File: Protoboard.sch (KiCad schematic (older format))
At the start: 7 parts

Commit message: Updated footprints for most things.
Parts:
- added D1, D2: D, Diodes_SMD:SOD-323_HandSoldering, symbol D
- added R3: 10k, Resistors_SMD:R_1206_HandSoldering, symbol R
- P1: renamed from P?; footprint (none) -> Connectors_Molex:Molex_PicoBlade_53261-0871_08x1.25mm_Angled
- P2, P4: renamed from P?; footprint (none) -> Pin_Headers:Pin_Header_Straight_1x04
- P3: renamed from P?; footprint (none) -> Connectors_JST:JST_XH_S05B-XH-A_05x2.50mm_Angled
- R1, R2: renamed from R?; footprint (none) -> Resistors_SMD:R_1206_HandSoldering
- gave numbers to parts that had none: 1
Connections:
- net +3.3V: now also D1.1 (K)
- net +5V: now also R3.1
- new net DIN: D1.2 (A), D2.2 (A), R3.2
- new net LED: D2.1 (K)
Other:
- note added: "Level Converter for WS2812\n"
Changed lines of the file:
@@
 LIBS:contrib
 LIBS:valves
+LIBS:Protoboard-cache
 EELAYER 25 0
 EELAYER END
@@
 $EndDescr
 $Comp
-L CONN_01X04 P?
+L CONN_01X04 P2
 U 1 1 58C45125
 P 1000 1050
-F 0 "P?" H 1000 1300 50  0000 C CNN
+F 0 "P2" H 1000 1300 50  0000 C CNN
 F 1 "CONN_01X04" V 1100 1050 50  0000 C CNN
-F 2 "" H 1000 1050 50  0000 C CNN
+F 2 "Pin_Headers:Pin_Header_Straight_1x04" H 1000 1050 50  0001 C CNN
 F 3 "" H 1000 1050 50  0000 C CNN
 	1    1000 1050
@@
 $EndComp
 $Comp
-L CONN_01X04 P?
+L CONN_01X04 P4
 U 1 1 58C4517D
 P 1600 1600
-F 0 "P?" H 1600 1850 50  0000 C CNN
+F 0 "P4" H 1600 1850 50  0000 C CNN
 F 1 "CONN_01X04" V 1700 1600 50  0000 C CNN
-F 2 "" H 1600 1600 50  0000 C CNN
+F 2 "Pin_Headers:Pin_Header_Straight_1x04" H 1600 1600 50  0001 C CNN
 F 3 "" H 1600 1600 50  0000 C CNN
 	1    1600 1600
@@
 I2C Sensor Connector\n
 $Comp
-L CONN_01X05 P?
+L CONN_01X05 P3
 U 1 1 58C45292
 P 1000 2500
-F 0 "P?" H 1000 2800 50  0000 C CNN
+F 0 "P3" H 1000 2800 50  0000 C CNN
 F 1 "CONN_01X05" V 1100 2500 50  0000 C CNN
-F 2 "" H 1000 2500 50  0000 C CNN
+F 2 "Connectors_JST:JST_XH_S05B-XH-A_05x2.50mm_Angled" H 1000 2500 50  0001 C CNN
 F 3 "" H 1000 2500 50  0000 C CNN
 	1    1000 2500
@@
 SDS011 Connector\n
 $Comp
-L CONN_02X05 P?
+L CONN_02X05 P5
 U 1 1 58C453D9
 P 3300 4400
-F 0 "P?" H 3300 4700 50  0000 C CNN
+F 0 "P5" H 3300 4700 50  0000 C CNN
 F 1 "CONN_02X05" H 3300 4100 50  0000 C CNN
-F 2 "" H 3300 3200 50  0000 C CNN
+F 2 "" H 3300 3200 50  0001 C CNN
 F 3 "" H 3300 3200 50  0000 C CNN
 	1    3300 4400
@@
 PMS7003 Connector\n
 $Comp
-L CONN_01X08 P?
+L CONN_01X08 P1
 U 1 1 58C459C6
 P 950 6250
-F 0 "P?" H 950 6700 50  0000 C CNN
+F 0 "P1" H 950 6700 50  0000 C CNN
 F 1 "CONN_01X08" V 1050 6250 50  0000 C CNN
-F 2 "" H 950 6250 50  0000 C CNN
+F 2 "Connectors_Molex:Molex_PicoBlade_53261-0871_08x1.25mm_Angled" H 950 6250 50  0001 C CNN
 F 3 "" H 950 6250 50  0000 C CNN
 	1    950  6250
@@
 RESET
 $Comp
-L R R?
+L R R2
 U 1 1 58C4605C
 P 6150 1700
-F 0 "R?" V 6230 1700 50  0000 C CNN
+F 0 "R2" V 6230 1700 50  0000 C CNN
 F 1 "10k" V 6150 1700 50  0000 C CNN
-F 2 "" V 6080 1700 50  0000 C CNN
+F 2 "Resistors_SMD:R_1206_HandSoldering" V 6080 1700 50  0001 C CNN
 F 3 "" H 6150 1700 50  0000 C CNN
 	1    6150 1700
@@
 $EndComp
 $Comp
-L R R?
+L R R1
 U 1 1 58C4608F
 P 6150 1200
-F 0 "R?" V 6230 1200 50  0000 C CNN
+F 0 "R1" V 6230 1200 50  0000 C CNN
 F 1 "10k" V 6150 1200 50  0000 C CNN
-F 2 "" V 6080 1200 50  0000 C CNN
+F 2 "Resistors_SMD:R_1206_HandSoldering" V 6080 1200 50  0001 C CNN
 F 3 "" H 6150 1200 50  0000 C CNN
 	1    6150 1200
@@
 Text Notes 5400 950  0    60   ~ 0
 Pullups for PMS Sensors\n
+$Comp
+L D D1
+U 1 1 58C46C46
+P 6150 2500
+F 0 "D1" H 6150 2600 50  0000 C CNN
+F 1 "D" H 6150 2400 50  0000 C CNN
+F 2 "Diodes_SMD:SOD-323_HandSoldering" H 6150 2500 50  0001 C CNN
+F 3 "" H 6150 2500 50  0000 C CNN
+	1    6150 2500
+	1    0    0    -1
+$EndComp
+$Comp
+L D D2
+U 1 1 58C46CBC
+P 6150 3100
+F 0 "D2" H 6150 3200 50  0000 C CNN
+F 1 "D" H 6150 3000 50  0000 C CNN
+F 2 "Diodes_SMD:SOD-323_HandSoldering" H 6150 3100 50  0001 C CNN
+F 3 "" H 6150 3100 50  0000 C CNN
+	1    6150 3100
+	1    0    0    -1
+$EndComp
+Text GLabel 7200 3100 2    60   Input ~ 0
+DIN
+Text GLabel 7200 2500 2    60   Input ~ 0
++5V
+$Comp
+L R R3
+U 1 1 58C46D88
+P 6750 2500
+F 0 "R3" V 6830 2500 50  0000 C CNN
+F 1 "10k" V 6750 2500 50  0000 C CNN
+F 2 "Resistors_SMD:R_1206_HandSoldering" V 6680 2500 50  0001 C CNN
+F 3 "" H 6750 2500 50  0000 C CNN
+	1    6750 2500
+	0    1    1    0
+$EndComp
+Wire Wire Line
+	6900 2500 7200 2500
+Wire Wire Line
+	6600 2500 6300 2500
+Wire Wire Line
+	6300 3100 7200 3100
+Wire Wire Line
+	6450 2500 6450 3100
+Connection ~ 6450 3100
+Connection ~ 6450 2500
+Text GLabel 5400 2500 0    60   Input ~ 0
++3.3V
+Wire Wire Line
+	5400 2500 6000 2500
+Text GLabel 5400 3100 0    60   Input ~ 0
+LED
+Wire Wire Line
+	5400 3100 6000 3100
+Text Notes 5250 2300 0    60   ~ 0
+Level Converter for WS2812\n
 $EndSCHEMATC

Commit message: Added a drawing for RS part no http://uk.rs-online.com/web/p/pcb-sockets/7944590/?sra=pstk
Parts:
- P5: footprint (none) -> Amphenol:Amphenol
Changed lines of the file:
@@
 F 0 "P5" H 3300 4700 50  0000 C CNN
 F 1 "CONN_02X05" H 3300 4100 50  0000 C CNN
-F 2 "" H 3300 3200 50  0001 C CNN
+F 2 "Amphenol:Amphenol" H 3300 3200 50  0001 C CNN
 F 3 "" H 3300 3200 50  0000 C CNN
 	1    3300 4400

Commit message: WIP
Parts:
- added P6: CONN_01X10, Pin_Headers:Pin_Header_Straight_1x10, symbol CONN_01X10
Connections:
- net +3.3V: now also P6.3 (P3)
- net +5V: now also P6.4 (P4)
- net DIN: now also P6.10 (P10)
- net GND: now also P6.5 (P5)
- net RESET: now also P6.9 (P9)
- net RXD: now also P6.7 (P7)
- net SCL: now also P6.1 (P1)
- net SDA: now also P6.2 (P2)
- net SET: now also P6.8 (P8)
- net TXD: now also P6.6 (P6)
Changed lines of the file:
@@
 Text Notes 5250 2300 0    60   ~ 0
 Level Converter for WS2812\n
+Text GLabel 8100 3450 0    60   Input ~ 0
+SCL
+Text GLabel 8100 3600 0    60   Input ~ 0
+SDA
+Text GLabel 8100 3750 0    60   Input ~ 0
++3.3V
+Text GLabel 8100 3900 0    60   Input ~ 0
++5V
+Text GLabel 8100 4050 0    60   Input ~ 0
+GND
+Text GLabel 8100 4200 0    60   Input ~ 0
+TXD
+Text GLabel 8100 4350 0    60   Input ~ 0
+RXD
+Text GLabel 8100 4500 0    60   Input ~ 0
+SET
+Text GLabel 8100 4650 0    60   Input ~ 0
+RESET
+Text GLabel 8100 4800 0    60   Input ~ 0
+DIN
+$Comp
+L CONN_01X10 P6
+U 1 1 58C59B8A
+P 9350 4150
+F 0 "P6" H 9350 4700 50  0000 C CNN
+F 1 "CONN_01X10" V 9450 4150 50  0000 C CNN
+F 2 "Pin_Headers:Pin_Header_Straight_1x10" H 9350 4150 50  0001 C CNN
+F 3 "" H 9350 4150 50  0000 C CNN
+	1    9350 4150
+	1    0    0    -1
+$EndComp
+Wire Wire Line
+	9150 3700 9050 3700
+Wire Wire Line
+	9050 3700 9050 3450
+Wire Wire Line
+	9050 3450 8100 3450
+Wire Wire Line
+	9150 3800 8950 3800
+Wire Wire Line
+	8950 3800 8950 3600
+Wire Wire Line
+	8950 3600 8100 3600
+Wire Wire Line
+	9150 3900 8850 3900
+Wire Wire Line
+	8850 3900 8850 3750
+Wire Wire Line
+	8850 3750 8100 3750
+Wire Wire Line
+	9150 4000 8750 4000
+Wire Wire Line
+	8750 4000 8750 3900
+Wire Wire Line
+	8750 3900 8100 3900
+Wire Wire Line
+	9150 4100 8650 4100
+Wire Wire Line
+	8650 4100 8650 4050
+Wire Wire Line
+	8650 4050 8100 4050
+Wire Wire Line
+	9150 4200 8100 4200
+Wire Wire Line
+	9150 4300 8650 4300
+Wire Wire Line
+	8650 4300 8650 4350
+Wire Wire Line
+	8650 4350 8100 4350
+Wire Wire Line
+	9150 4400 8750 4400
+Wire Wire Line
+	8750 4400 8750 4500
+Wire Wire Line
+	8750 4500 8100 4500
+Wire Wire Line
+	9150 4500 8850 4500
+Wire Wire Line
+	8850 4500 8850 4650
+Wire Wire Line
+	8850 4650 8100 4650
+Wire Wire Line
+	9150 4600 8950 4600
+Wire Wire Line
+	8950 4600 8950 4800
+Wire Wire Line
+	8950 4800 8100 4800
 $EndSCHEMATC

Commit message: Routing done.
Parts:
- removed P4: CONN_01X04, Pin_Headers:Pin_Header_Straight_1x04, symbol CONN_01X04
- removed P6: CONN_01X10, Pin_Headers:Pin_Header_Straight_1x10, symbol CONN_01X10
- added P4: CONN_01X11, Pin_Headers:Pin_Header_Straight_1x11, symbol CONN_01X11
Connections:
- net +3.3V: now also P4.3 (P3)
- net +5V: now also P4.5 (P5)
- net DIN: now also P4.10 (P10)
- net GND: now also P4.4 (P4)
- net LED: now also P4.11 (P11)
- net RESET: now also P4.9 (P9)
- net RXD: now also P4.7 (P7)
- net SCL: now also P4.1 (P1)
- net SDA: now also P4.2 (P2)
- net SET: now also P4.6 (P6)
- net TXD: now also P4.8 (P8)
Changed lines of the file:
@@
 	-1   0    0    1
-$EndComp
-$Comp
-L CONN_01X04 P4
-U 1 1 58C4517D
-P 1600 1600
-F 0 "P4" H 1600 1850 50  0000 C CNN
-F 1 "CONN_01X04" V 1700 1600 50  0000 C CNN
-F 2 "Pin_Headers:Pin_Header_Straight_1x04" H 1600 1600 50  0001 C CNN
-F 3 "" H 1600 1600 50  0000 C CNN
-	1    1600 1600
-	0    1    1    0
 $EndComp
 Text GLabel 2400 1200 2    60   Input ~ 0
@@
 	1200 1200 2400 1200
 Wire Wire Line
-	1750 1400 1750 1200
-Connection ~ 1750 1200
-Wire Wire Line
 	1200 1100 2750 1100
 Wire Wire Line
-	1650 1400 1650 1100
-Connection ~ 1650 1100
-Wire Wire Line
-	2400 1000 1200 1000
-Wire Wire Line
-	1450 1400 1450 1000
-Connection ~ 1450 1000
-Wire Wire Line
 	2750 900  1200 900
-Wire Wire Line
-	1550 1400 1550 900
-Connection ~ 1550 900
 Text Notes 1400 850  0    60   ~ 0
 I2C Sensor Connector\n
@@
 Text GLabel 8100 3750 0    60   Input ~ 0
 +3.3V
+Text GLabel 8100 4050 0    60   Input ~ 0
++5V
 Text GLabel 8100 3900 0    60   Input ~ 0
-+5V
-Text GLabel 8100 4050 0    60   Input ~ 0
-GND
-Text GLabel 8100 4200 0    60   Input ~ 0
+GND
+Text GLabel 8100 4500 0    60   Input ~ 0
 TXD
 Text GLabel 8100 4350 0    60   Input ~ 0
 RXD
-Text GLabel 8100 4500 0    60   Input ~ 0
+Text GLabel 8100 4200 0    60   Input ~ 0
 SET
 Text GLabel 8100 4650 0    60   Input ~ 0
@@
 Text GLabel 8100 4800 0    60   Input ~ 0
 DIN
-$Comp
-L CONN_01X10 P6
-U 1 1 58C59B8A
-P 9350 4150
-F 0 "P6" H 9350 4700 50  0000 C CNN
-F 1 "CONN_01X10" V 9450 4150 50  0000 C CNN
-F 2 "Pin_Headers:Pin_Header_Straight_1x10" H 9350 4150 50  0001 C CNN
-F 3 "" H 9350 4150 50  0000 C CNN
-	1    9350 4150
+Text GLabel 8100 4950 0    60   Input ~ 0
+LED
+Wire Wire Line
+	2400 1000 1200 1000
+$Comp
+L CONN_01X11 P4
+U 1 1 58C5C7BE
+P 9200 4200
+F 0 "P4" H 9200 4800 50  0000 C CNN
+F 1 "CONN_01X11" V 9300 4200 50  0000 C CNN
+F 2 "Pin_Headers:Pin_Header_Straight_1x11" H 9200 4200 50  0001 C CNN
+F 3 "" H 9200 4200 50  0000 C CNN
+	1    9200 4200
 	1    0    0    -1
 $EndComp
 Wire Wire Line
-	9150 3700 9050 3700
-Wire Wire Line
-	9050 3700 9050 3450
-Wire Wire Line
-	9050 3450 8100 3450
-Wire Wire Line
-	9150 3800 8950 3800
-Wire Wire Line
-	8950 3800 8950 3600
-Wire Wire Line
-	8950 3600 8100 3600
-Wire Wire Line
-	9150 3900 8850 3900
-Wire Wire Line
-	8850 3900 8850 3750
-Wire Wire Line
-	8850 3750 8100 3750
-Wire Wire Line
-	9150 4000 8750 4000
-Wire Wire Line
-	8750 4000 8750 3900
-Wire Wire Line
-	8750 3900 8100 3900
-Wire Wire Line
-	9150 4100 8650 4100
-Wire Wire Line
-	8650 4100 8650 4050
-Wire Wire Line
-	8650 4050 8100 4050
-Wire Wire Line
-	9150 4200 8100 4200
-Wire Wire Line
-	9150 4300 8650 4300
-Wire Wire Line
-	8650 4300 8650 4350
-Wire Wire Line
-	8650 4350 8100 4350
-Wire Wire Line
-	9150 4400 8750 4400
-Wire Wire Line
-	8750 4400 8750 4500
-Wire Wire Line
-	8750 4500 8100 4500
-Wire Wire Line
-	9150 4500 8850 4500
-Wire Wire Line
-	8850 4500 8850 4650
-Wire Wire Line
-	8850 4650 8100 4650
-Wire Wire Line
-	9150 4600 8950 4600
-Wire Wire Line
-	8950 4600 8950 4800
-Wire Wire Line
-	8950 4800 8100 4800
+	8100 3450 9000 3450
+Wire Wire Line
+	9000 3450 9000 3700
+Wire Wire Line
+	9000 3800 8900 3800
+Wire Wire Line
+	8900 3800 8900 3600
+Wire Wire Line
+	8900 3600 8100 3600
+Wire Wire Line
+	9000 3900 8800 3900
+Wire Wire Line
+	8800 3900 8800 3750
+Wire Wire Line
+	8800 3750 8100 3750
+Wire Wire Line
+	8100 3900 8700 3900
+Wire Wire Line
+	8700 3900 8700 4000
+Wire Wire Line
+	8700 4000 9000 4000
+Wire Wire Line
+	9000 4100 8600 4100
+Wire Wire Line
+	8600 4100 8600 4050
+Wire Wire Line
+	8600 4050 8100 4050
+Wire Wire Line
+	9000 4200 8100 4200
+Wire Wire Line
+	9000 4300 8600 4300
+Wire Wire Line
+	8600 4300 8600 4350
+Wire Wire Line
+	8600 4350 8100 4350
+Wire Wire Line
+	8100 4500 8700 4500
+Wire Wire Line
+	8700 4500 8700 4400
+Wire Wire Line
+	8700 4400 9000 4400
+Wire Wire Line
+	9000 4500 8800 4500
+Wire Wire Line
+	8800 4500 8800 4650
+Wire Wire Line
+	8800 4650 8100 4650
+Wire Wire Line
+	9000 4600 8900 4600
+Wire Wire Line
+	8900 4600 8900 4800
+Wire Wire Line
+	8900 4800 8100 4800
+Wire Wire Line
+	9000 4700 9000 4950
+Wire Wire Line
+	9000 4950 8100 4950
 $EndSCHEMATC

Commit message: Reorganized board, fixed bug with Molex Microblade connector (reversed pins).
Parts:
- P3: footprint Connectors_JST:JST_XH_S05B-XH-A_05x2.50mm_Angled -> Connectors_JST:JST_XH_B05B-XH-A_05x2.50mm_Straight
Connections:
- net +5V: now also P1.8 (P8); no longer P1.1 (P1)
- net GND: now also P1.7 (P7); no longer P1.2 (P2)
- net RESET: now also P1.3 (P3); no longer P1.6 (P6)
- net RXD: now also P1.5 (P5); no longer P1.4 (P4)
- net SET: now also P1.6 (P6); no longer P1.3 (P3)
- net TXD: now also P1.4 (P4); no longer P1.5 (P5)
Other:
- note added: "Note the pins on this connector are reversed to what is in the datasheet for the PMS5003\n"
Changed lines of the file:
@@
 F 0 "P3" H 1000 2800 50  0000 C CNN
 F 1 "CONN_01X05" V 1100 2500 50  0000 C CNN
-F 2 "Connectors_JST:JST_XH_S05B-XH-A_05x2.50mm_Angled" H 1000 2500 50  0001 C CNN
+F 2 "Connectors_JST:JST_XH_B05B-XH-A_05x2.50mm_Straight" H 1000 2500 50  0001 C CNN
 F 3 "" H 1000 2500 50  0000 C CNN
 	1    1000 2500
@@
 	-1   0    0    1
 $EndComp
-Text GLabel 2450 6600 2    60   Input ~ 0
-+5V
-Text GLabel 2800 6500 2    60   Input ~ 0
+Text GLabel 2800 5900 2    60   Input ~ 0
++5V
+Text GLabel 2450 6000 2    60   Input ~ 0
 GND
-Wire Wire Line
-	2450 6600 1150 6600
-Wire Wire Line
-	1150 6500 2800 6500
+Text GLabel 3200 6100 2    60   Input ~ 0
+SET
+Wire Wire Line
+	3200 6400 1150 6400
+Text GLabel 2800 6200 2    60   Input ~ 0
+RXD
+Text GLabel 2450 6300 2    60   Input ~ 0
+TXD
+Wire Wire Line
+	2450 6300 1150 6300
+Wire Wire Line
+	1150 6200 2800 6200
 Text GLabel 3200 6400 2    60   Input ~ 0
-SET
-Wire Wire Line
-	3200 6400 1150 6400
-Text GLabel 2450 6300 2    60   Input ~ 0
-RXD
-Text GLabel 2800 6200 2    60   Input ~ 0
-TXD
-Wire Wire Line
-	2450 6300 1150 6300
-Wire Wire Line
-	1150 6200 2800 6200
-Text GLabel 3200 6100 2    60   Input ~ 0
 RESET
 Wire Wire Line
@@
 Wire Wire Line
 	9000 4950 8100 4950
+Text Notes 1000 6950 0    60   ~ 0
+Note the pins on this connector are reversed to what is in the datasheet for the PMS5003\n
+Wire Wire Line
+	1150 5900 2800 5900
+Wire Wire Line
+	2450 6000 1150 6000
 $EndSCHEMATC

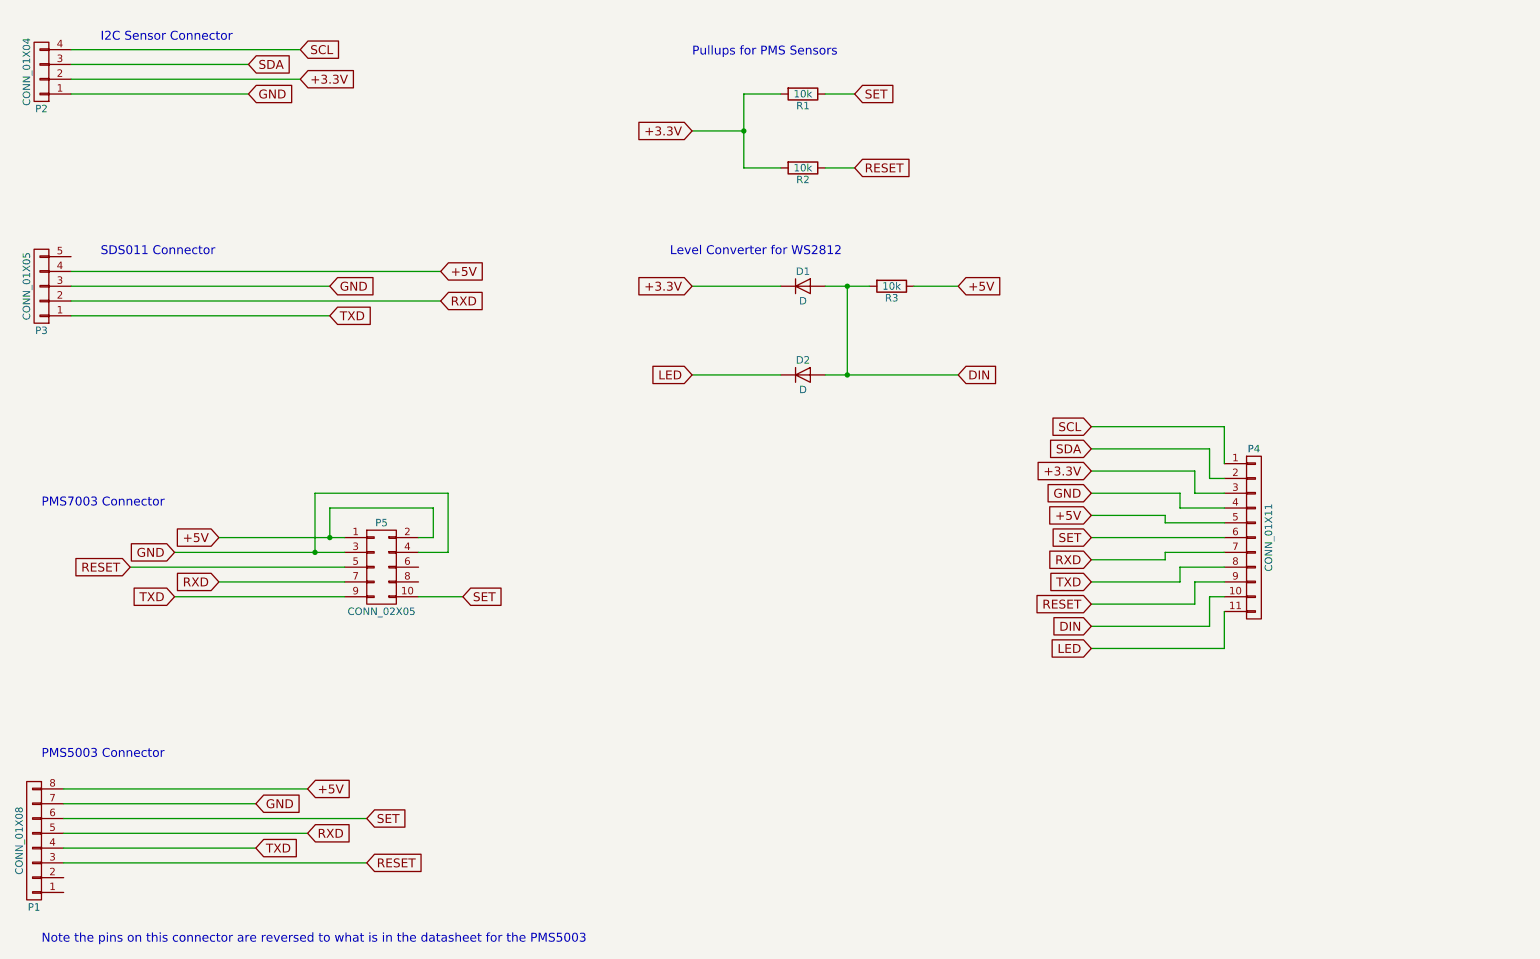
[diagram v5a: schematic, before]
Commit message: Added WS2812B leds.
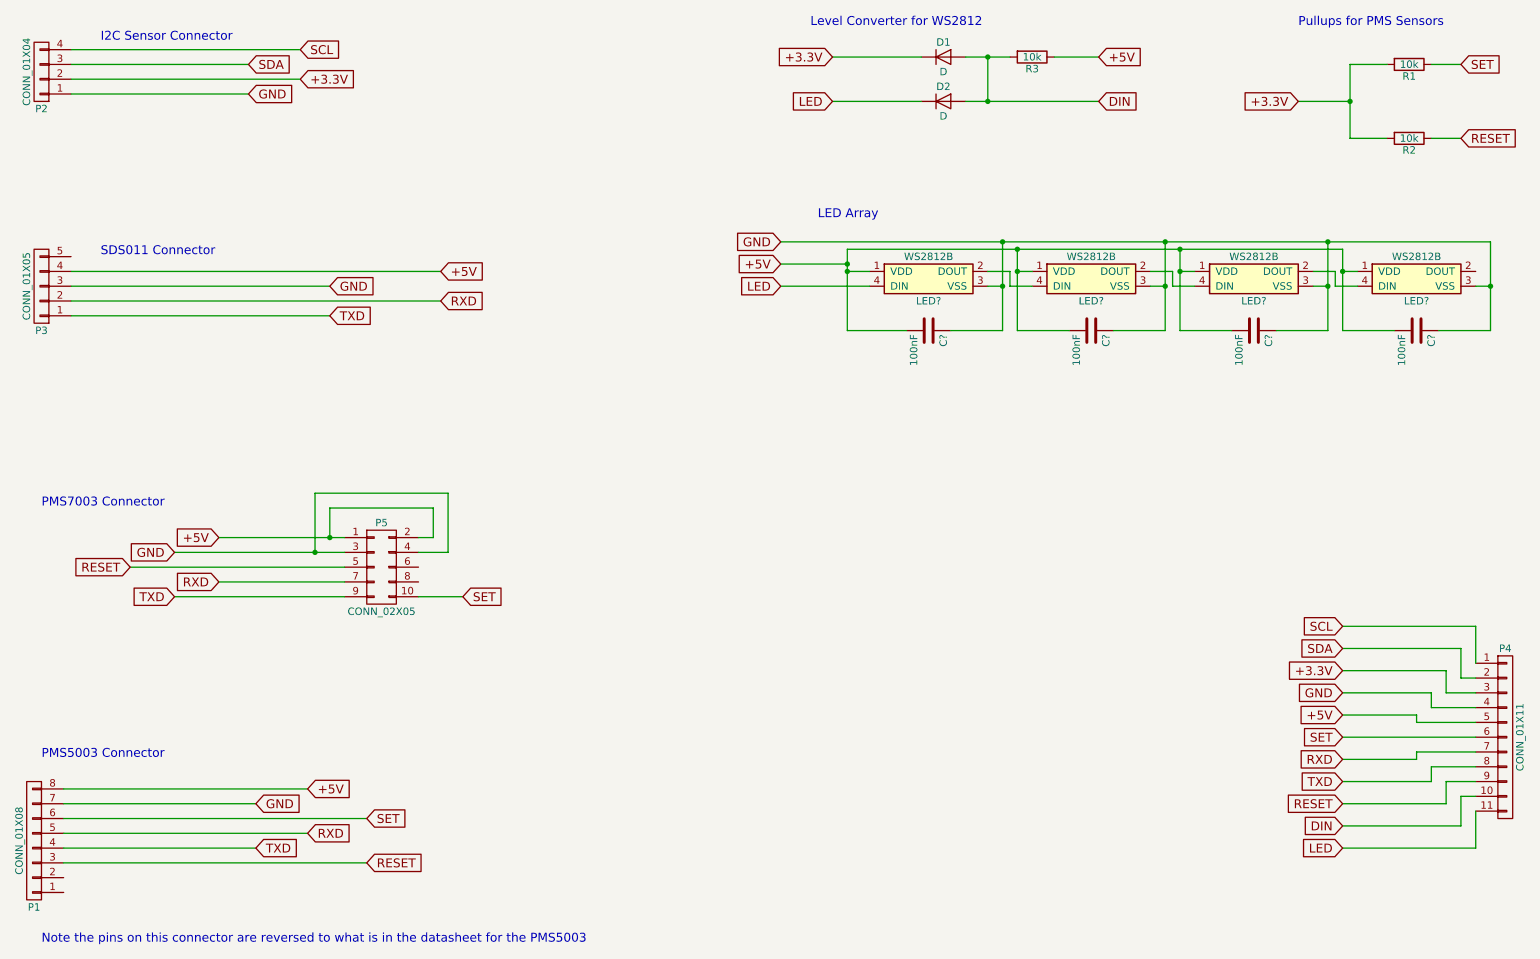
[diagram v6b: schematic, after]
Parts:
- added C? (x4): 100nF, symbol C
- added LED? (x4): WS2812B, LEDs:LED_WS2812B-PLCC4, symbol WS2812B
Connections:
- net +5V: now also C?.2, C?.2, C?.2, C?.2, LED?.1 (VDD), LED?.1 (VDD), LED?.1 (VDD), LED?.1 (VDD)
- net GND: now also C?.1, C?.1, C?.1, C?.1, LED?.3 (VSS), LED?.3 (VSS), LED?.3 (VSS), LED?.3 (VSS)
- net LED: now also LED?.4 (DIN)
- new net: LED?.2 (DOUT), LED?.4 (DIN) (x3)
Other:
- note added: "LED Array\n"
- moved on the sheet: D1, D2, P4, R1, R2, R3
